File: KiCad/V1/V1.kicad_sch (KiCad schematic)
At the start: 65 parts, among them Q1 Q_NMOS_GSD, Q2 Q_NMOS_GSD, U1 LMG1210RVRR, U2 OPA2677IDDA, U3 OPA2677IDDA, U4 OPA859QDSGRQ1, U5 OPA859QDSGRQ1, U6 OPA859QDSGRQ1

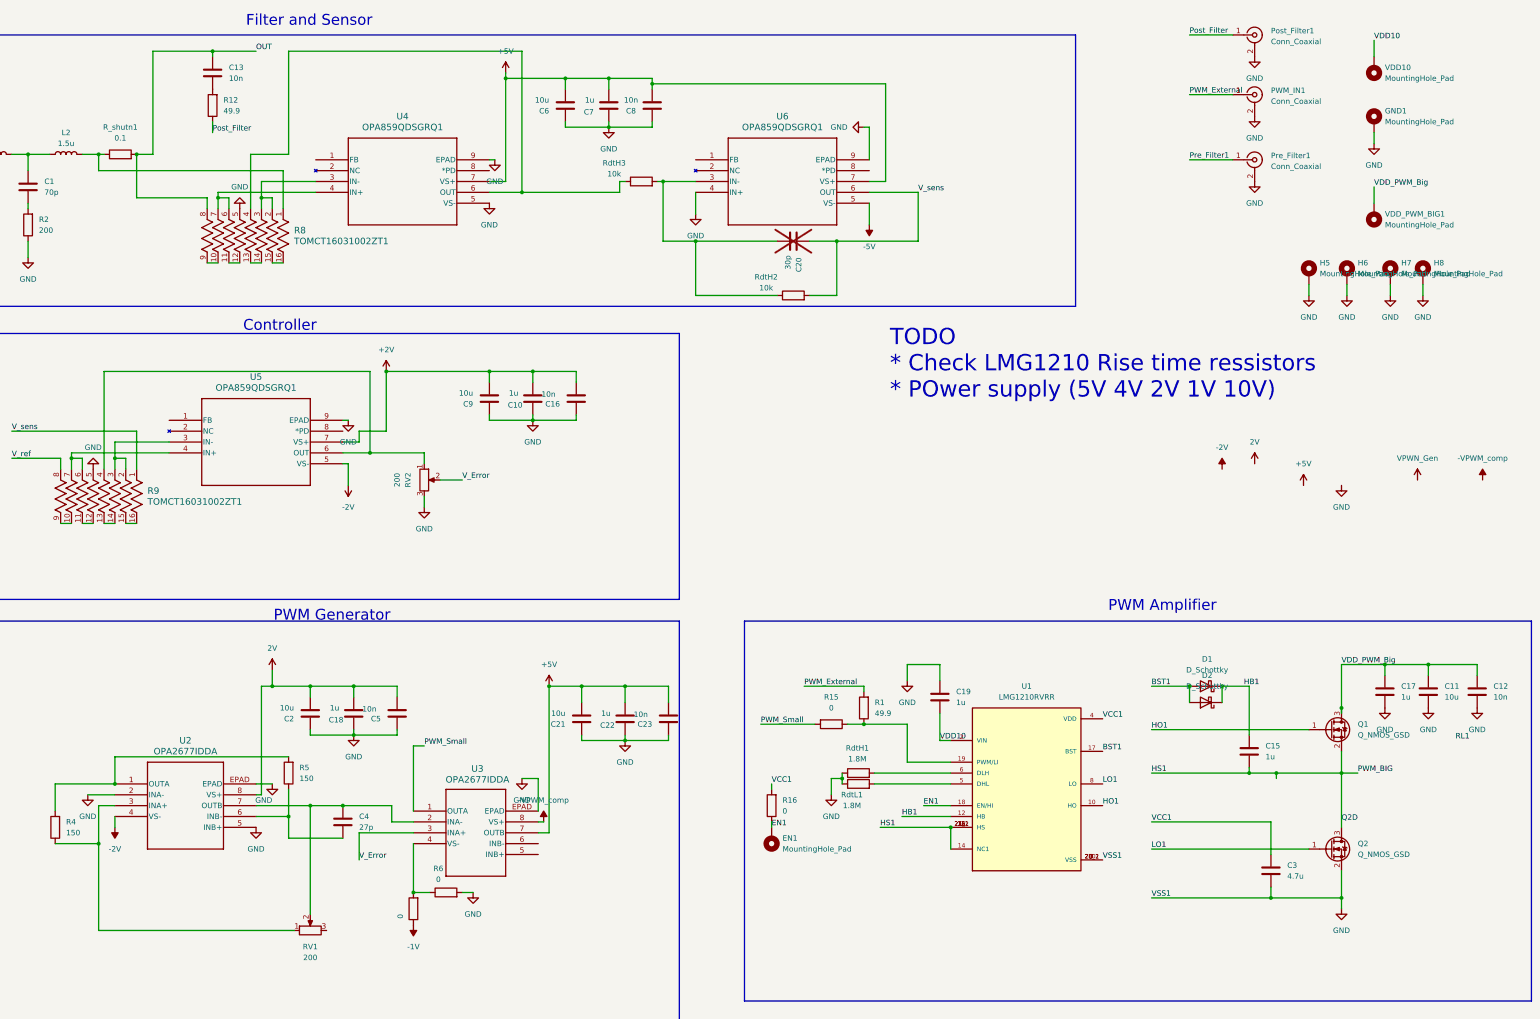
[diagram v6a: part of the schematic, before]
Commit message: added integrator
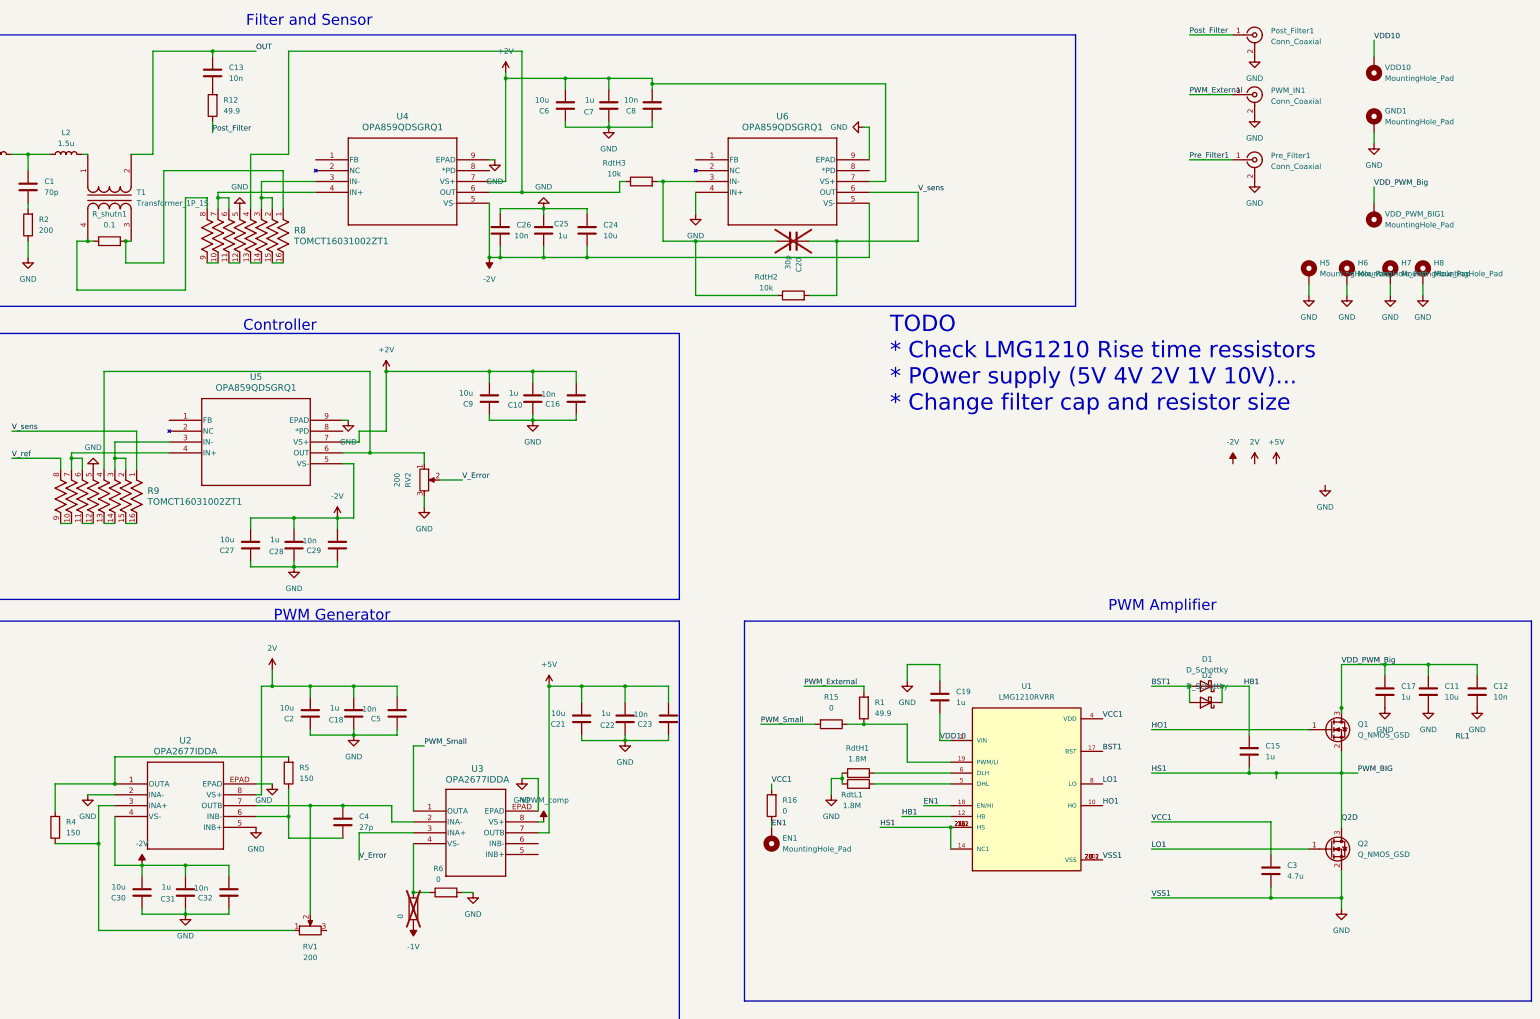
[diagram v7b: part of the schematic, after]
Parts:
- added C24, C27: 10u, Capacitor_SMD:C_0603_1608Metric, symbol Device:C
- added C25, C28, C31: 1u, Capacitor_SMD:C_0402_1005Metric, symbol Device:C
- added C26, C29, C32: 10n, Capacitor_SMD:C_0402_1005Metric, symbol Device:C
- added C30: 10u, Capacitor_SMD:C_0402_1005Metric, symbol Device:C
- added T1: Transformer_1P_1S, symbol Device:Transformer_1P_1S
- R3: now not fitted
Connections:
- net -5V is gone; now on net -2V: U6.5 (VS-)
- net +2V: now also C6.2, C7.2, C8.2, U4.7 (VS+), U6.7 (VS+)
- net +5V: no longer C6.2, C7.2, C8.2, U4.7 (VS+), U6.7 (VS+)
- net -2V: now also U4.5 (VS-), C24.2, C25.2, C26.2, C27.2, C28.2, C29.2, C30.2, C31.2, C32.2
- net GND: now also C24.1, C25.1, C26.1, C27.1, C28.1, C29.1, C30.1, C31.1, C32.1; no longer U4.5 (VS-)
- net OUT: now also T1.2 (AB); no longer R8.8, R_shutn1.2
- new net: R8.1, R_shutn1.2, T1.3 (SA)
- new net: R8.8, R_shutn1.1, T1.4 (SB)
- new net: L2.2, T1.1 (AA)
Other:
- note added: "TODO * Check LMG1210 Rise time ressistors * POwer supply (5V 4V 2V 1V 10V)... * Change filter cap and resistor size"
- note removed: "TODO * Check LMG1210 Rise time ressistors * POwer supply (5V 4V 2V 1V 10V)"

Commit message: V1 pcb almost done
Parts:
- removed RdtH2, RdtH3: 10k, Resistor_SMD:R_0402_1005Metric, symbol Device:R
- added EN1, Pre_FilterV_duffsense, Pre_FilterV_ref: Conn_Coaxial, Connector_Coaxial:U.FL_Molex_MCRF_73412-0110_Vertical, symbol Connector:Conn_Coaxial
- added R10, R13, R7: 150, Resistor_SMD:R_0402_1005Metric, symbol Device:R
- added R11: 10k, Resistor_SMD:R_0402_1005Metric, symbol Device:R
- added VDD2, VDD3, VDD4: MountingHole_Pad, TestPoint:TestPoint_THTPad_D2.5mm_Drill1.2mm, symbol Mechanical:MountingHole_Pad
- added VDD_PWM_BIG2, VDD_PWM_BIG3: MountingHole_Pad, MountingHole:MountingHole_2.5mm_Pad_TopBottom, symbol Mechanical:MountingHole_Pad
- R8, R9: footprint MyFootprints:TOMCT16031002ZT1 -> MyFootprints:NOMCT16031
- R_shutn1: footprint Resistor_SMD:R_2512_6332Metric -> Resistor_SMD:R_1020_2550Metric_Pad1.33x5.20mm_HandSolder
- renumbered PWM_IN1 to PWM_External
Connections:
- net -VPWM_comp is gone; now on net +5V: U3.8 (VS+)
- net 2V is gone; now on net +2V: C18.2, C2.2, C5.2, U2.8 (VS+)
- net +2V: now also VDD3.1
- net +5V: now also VDD4.1; no longer U3.7 (OUTB)
- net -2V: now also VDD2.1
- net EN1: now also EN1.1 (In)
- net GND: now also U3.5 (INB+), EN1.2 (Ext), Pre_FilterV_duffsense.2 (Ext), Pre_FilterV_ref.2 (Ext), R11.2
- net HS1: now also R11.1
- net V_ref: now also Pre_FilterV_ref.1 (In)
- net V_sens: now also R10.1
- net at C4.2, RV1.2, U2.7 (OUTB): now also R13.2; no longer U3.2 (INA-)
- net at C20.2, U6.3 (IN-): now also R10.2, R7.1
- net V_diffsense: now reaches R8.4, U4.6 (OUT)
- net V_diffsense: now also Pre_FilterV_duffsense.1 (In), R7.2
- net at U3.6 (INB-): now also U3.7 (OUTB)
- new net: R13.1, U3.2 (INA-)
- new net +I_OUT: VDD_PWM_BIG2.1
- new net -I_OUT: VDD_PWM_BIG3.1
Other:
- note removed: "TODO * Check LMG1210 Rise time ressistors * POwer supply (5V 4V 2V 1V 10V)... * Change filter cap and resistor size"
- moved on the sheet: EN1, H5, H6, H7, H8, R16, VDD_PWM_BIG1
